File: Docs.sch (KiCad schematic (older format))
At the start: 0 parts

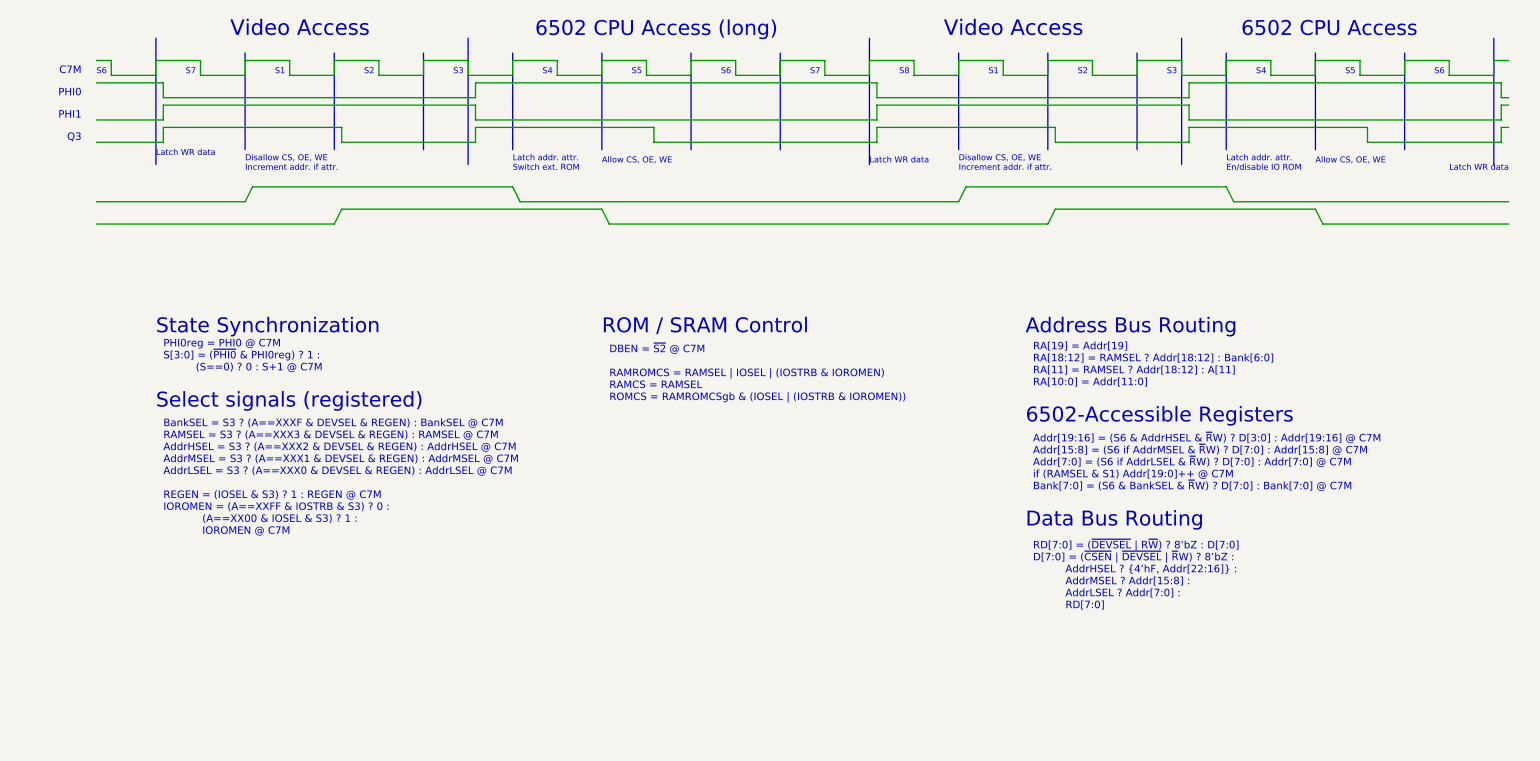
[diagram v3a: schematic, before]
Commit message: Changed libraries
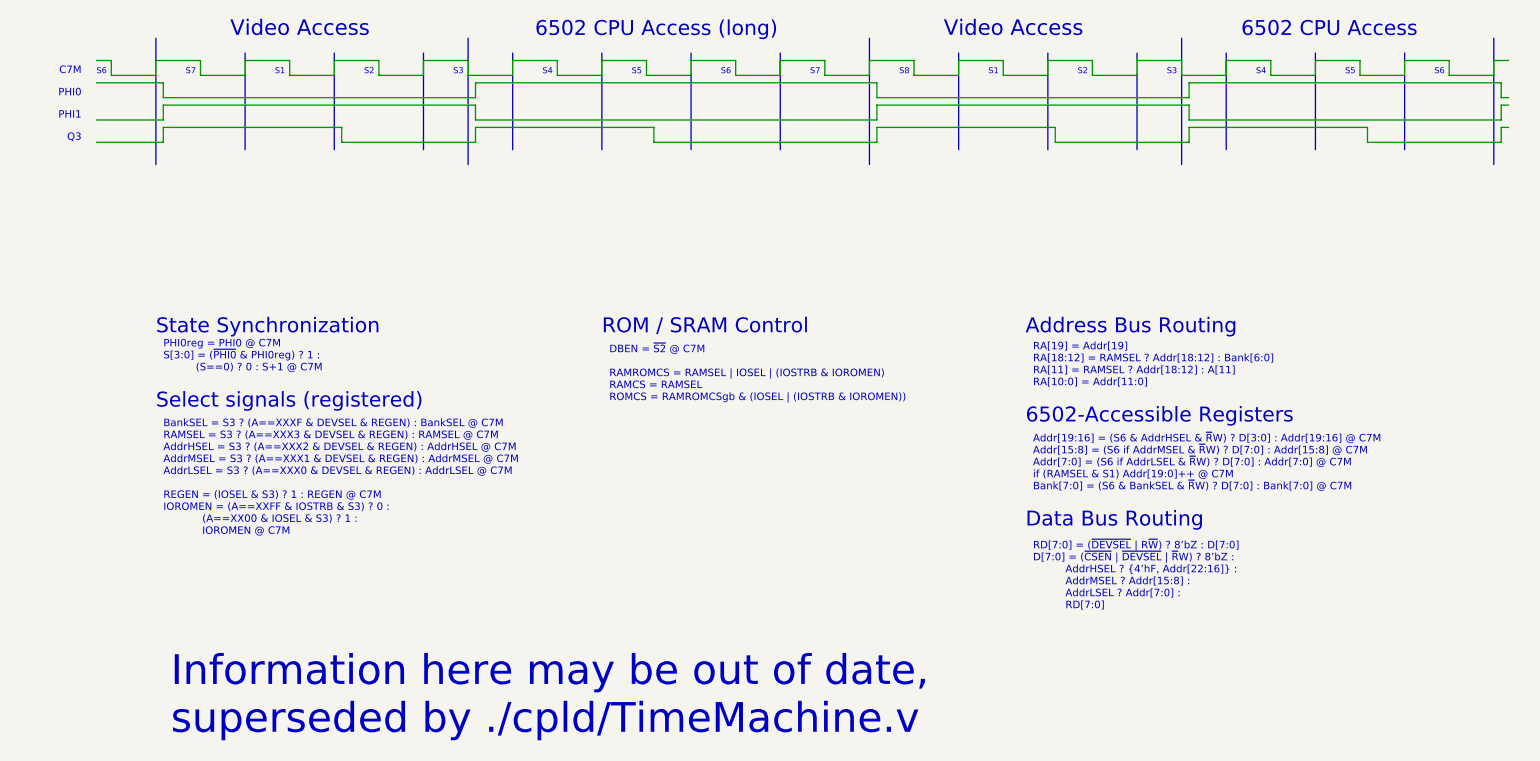
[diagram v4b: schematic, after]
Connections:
- wire segments 124 -> 106
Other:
- note added: "Information here may be out of date,\nsuperseded by ./cpld/TimeMachine.v"
- note removed: "Allow CS, OE, WE"
- note removed: "Disallow CS, OE, WE\nIncrement addr. if attr."
- note removed: "Latch WR data"
- note removed: "Latch addr. attr.\nEn/disable IO ROM"
- note removed: "Latch addr. attr.\nSwitch ext. ROM"
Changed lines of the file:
@@
 encoding utf-8
 Sheet 2 2
-Title "GR8RAM"
-Date "2019-07-23"
-Rev "0.1"
+Title "Time Machine"
+Date "2019-10-13"
+Rev "0.9"
 Comp "Garrett's Workshop"
 Comment1 ""
@@
 Wire Bus Line
 	4900 950  4900 1600
-Text Notes 4300 1700 0    40   ~ 0
-Allow CS, OE, WE
 Text Notes 1500 1100 0    40   ~ 0
 S7
@@
 Wire Bus Line
 	6100 850  6100 1700
-Text Notes 6100 1700 0    40   ~ 0
-Latch WR data
 Text Notes 6300 1100 0    40   ~ 0
 S8
@@
 Text Notes 8100 1100 0    40   ~ 0
 S3
-Text Notes 9100 1700 0    40   ~ 0
-Allow CS, OE, WE
 Text Notes 8700 1100 0    40   ~ 0
 S4
@@
 Wire Bus Line
 	1300 850  1300 1700
-Text Notes 1300 1650 0    40   ~ 0
-Latch WR data
 Text Notes 5100 1100 0    40   ~ 0
 S6
@@
 Wire Wire Line
 	5200 1000 5200 1100
+Wire Wire Line
+	10300 1000 10400 1000
+Wire Wire Line
+	10350 1250 10400 1250
+Wire Wire Line
+	10350 1300 10400 1300
+Wire Wire Line
+	10350 1450 10400 1450
+Text Notes 4350 3300 0    50   ~ 0
+DBEN = ~S2~ @ C7M\n\nRAMROMCS = RAMSEL | IOSEL | (IOSTRB & IOROMEN)\nRAMCS = RAMSEL\nROMCS = RAMROMCSgb & (IOSEL | (IOSTRB & IOROMEN))
+Text Notes 7200 3900 0    50   ~ 0
+Addr[19:16] = (S6 & AddrHSEL & ~R~W) ? D[3:0] : Addr[19:16] @ C7M\nAddr[15:8] = (S6 if AddrMSEL & ~R~W) ? D[7:0] : Addr[15:8] @ C7M\nAddr[7:0] = (S6 if AddrLSEL & ~R~W) ? D[7:0] : Addr[7:0] @ C7M\nif (RAMSEL & S1) Addr[19:0]++ @ C7M\nBank[7:0] = (S6 & BankSEL & ~R~W) ? D[7:0] : Bank[7:0] @ C7M
+Text Notes 7200 4700 0    50   ~ 0
+RD[7:0] = (~DEVSEL~ | R~W~) ? 8’bZ : D[7:0]\nD[7:0] = (~CSEN~ | ~DEVSEL~ | ~R~W) ? 8’bZ :\n          AddrHSEL ? {4’hF, Addr[22:16]} : \n          AddrMSEL ? Addr[15:8] : \n          AddrLSEL ? Addr[7:0] :\n          RD[7:0]
+Text Notes 7150 4150 0    100  ~ 0
+Data Bus Routing
+Text Notes 7150 3450 0    100  ~ 0
+6502-Accessible Registers
+Text Notes 7200 3200 0    50   ~ 0
+RA[19] = Addr[19]\nRA[18:12] = RAMSEL ? Addr[18:12] : Bank[6:0]\nRA[11] = RAMSEL ? Addr[18:12] : A[11]\nRA[10:0] = Addr[11:0]
+Text Notes 7150 2850 0    100  ~ 0
+Address Bus Routing
+Text Notes 1350 4200 0    50   ~ 0
+BankSEL = S3 ? (A==XXXF & DEVSEL & REGEN) : BankSEL @ C7M\nRAMSEL = S3 ? (A==XXX3 & DEVSEL & REGEN) : RAMSEL @ C7M\nAddrHSEL = S3 ? (A==XXX2 & DEVSEL & REGEN) : AddrHSEL @ C7M\nAddrMSEL = S3 ? (A==XXX1 & DEVSEL & REGEN) : AddrMSEL @ C7M\nAddrLSEL = S3 ? (A==XXX0 & DEVSEL & REGEN) : AddrLSEL @ C7M\n\nREGEN = (IOSEL & S3) ? 1 : REGEN @ C7M\nIOROMEN = (A==XXFF & IOSTRB & S3) ? 0 :\n            (A==XX00 & IOSEL & S3) ? 1 :\n            IOROMEN @ C7M
+Text Notes 4300 2850 0    100  ~ 0
+ROM / SRAM Control
+Text Notes 1300 2850 0    100  ~ 0
+State Synchronization
+Text Notes 1300 3350 0    100  ~ 0
+Select signals (registered)
 Text Notes 1350 3100 0    50   ~ 0
 PHI0reg = PHI0 @ C7M\nS[3:0] = (~PHI0~ & PHI0reg) ? 1 : \n          (S==0) ? 0 : S+1 @ C7M
-Text Notes 1300 3350 0    100  ~ 0
-Select signals (registered)
-Text Notes 1300 2850 0    100  ~ 0
-State Synchronization
-Text Notes 4300 2850 0    100  ~ 0
-ROM / SRAM Control
-Text Notes 1350 4200 0    50   ~ 0
-BankSEL = S3 ? (A==XXXF & DEVSEL & REGEN) : BankSEL @ C7M\nRAMSEL = S3 ? (A==XXX3 & DEVSEL & REGEN) : RAMSEL @ C7M\nAddrHSEL = S3 ? (A==XXX2 & DEVSEL & REGEN) : AddrHSEL @ C7M\nAddrMSEL = S3 ? (A==XXX1 & DEVSEL & REGEN) : AddrMSEL @ C7M\nAddrLSEL = S3 ? (A==XXX0 & DEVSEL & REGEN) : AddrLSEL @ C7M\n\nREGEN = (IOSEL & S3) ? 1 : REGEN @ C7M\nIOROMEN = (A==XXFF & IOSTRB & S3) ? 0 :\n            (A==XX00 & IOSEL & S3) ? 1 :\n            IOROMEN @ C7M
-Text Notes 7150 2850 0    100  ~ 0
-Address Bus Routing
-Wire Wire Line
-	10300 1000 10400 1000
-Wire Wire Line
-	10350 1250 10400 1250
-Wire Wire Line
-	10350 1300 10400 1300
-Wire Wire Line
-	10350 1450 10400 1450
-Text Notes 7200 3200 0    50   ~ 0
-RA[19] = Addr[19]\nRA[18:12] = RAMSEL ? Addr[18:12] : Bank[6:0]\nRA[11] = RAMSEL ? Addr[18:12] : A[11]\nRA[10:0] = Addr[11:0]
-Text Notes 10000 1750 0    40   ~ 0
-Latch WR data
-Text Notes 1900 1750 0    40   ~ 0
-Disallow CS, OE, WE\nIncrement addr. if attr.
-Text Notes 6700 1750 0    40   ~ 0
-Disallow CS, OE, WE\nIncrement addr. if attr.
-Text Notes 3700 1750 0    40   ~ 0
-Latch addr. attr.\nSwitch ext. ROM
-Text Notes 8500 1750 0    40   ~ 0
-Latch addr. attr.\nEn/disable IO ROM
-Text Notes 7150 3450 0    100  ~ 0
-6502-Accessible Registers
-Text Notes 7150 4150 0    100  ~ 0
-Data Bus Routing
-Text Notes 7200 4700 0    50   ~ 0
-RD[7:0] = (~DEVSEL~ | R~W~) ? 8’bZ : D[7:0]\nD[7:0] = (~CSEN~ | ~DEVSEL~ | ~R~W) ? 8’bZ :\n          AddrHSEL ? {4’hF, Addr[22:16]} : \n          AddrMSEL ? Addr[15:8] : \n          AddrLSEL ? Addr[7:0] :\n          RD[7:0]
-Text Notes 7200 3900 0    50   ~ 0
-Addr[19:16] = (S6 & AddrHSEL & ~R~W) ? D[3:0] : Addr[19:16] @ C7M\nAddr[15:8] = (S6 if AddrMSEL & ~R~W) ? D[7:0] : Addr[15:8] @ C7M\nAddr[7:0] = (S6 if AddrLSEL & ~R~W) ? D[7:0] : Addr[7:0] @ C7M\nif (RAMSEL & S1) Addr[19:0]++ @ C7M\nBank[7:0] = (S6 & BankSEL & ~R~W) ? D[7:0] : Bank[7:0] @ C7M
-Text Notes 4350 3300 0    50   ~ 0
-DBEN = ~S2~ @ C7M\n\nRAMROMCS = RAMSEL | IOSEL | (IOSTRB & IOROMEN)\nRAMCS = RAMSEL\nROMCS = RAMROMCSgb & (IOSEL | (IOSTRB & IOROMEN))
-Wire Wire Line
-	3700 1850 3750 1950
-Wire Wire Line
-	3750 1950 6700 1950
-Wire Wire Line
-	6700 1950 6750 1850
-Wire Wire Line
-	6750 1850 8500 1850
-Wire Wire Line
-	8500 1850 8550 1950
-Wire Wire Line
-	8550 1950 10400 1950
-Wire Wire Line
-	1950 1850 3700 1850
-Wire Wire Line
-	1950 1850 1900 1950
-Wire Wire Line
-	1900 1950 900  1950
-Wire Wire Line
-	4300 2000 4350 2100
-Wire Wire Line
-	4350 2100 7300 2100
-Wire Wire Line
-	7300 2100 7350 2000
-Wire Wire Line
-	7350 2000 9100 2000
-Wire Wire Line
-	9100 2000 9150 2100
-Wire Wire Line
-	9150 2100 10400 2100
-Wire Wire Line
-	2550 2000 4300 2000
-Wire Wire Line
-	2550 2000 2500 2100
-Wire Wire Line
-	900  2100 2500 2100
+Text Notes 1400 5550 0    200  ~ 0
+Information here may be out of date,\nsuperseded by ./cpld/TimeMachine.v
 $EndSCHEMATC

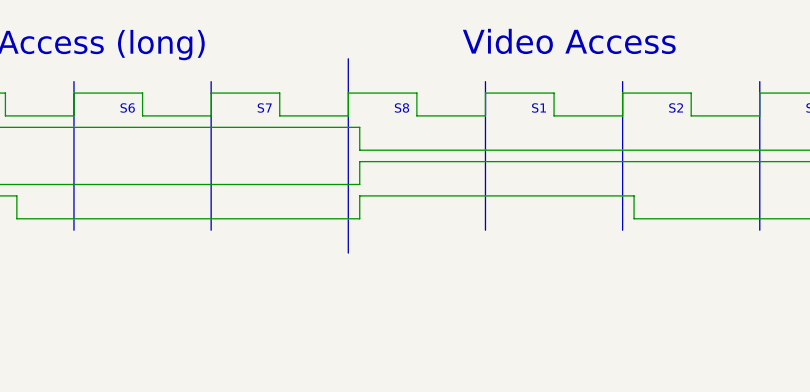
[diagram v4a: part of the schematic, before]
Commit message: New PLD revision
For write operations, register data is latched in the middle of S6, 70ns before the end of PHI0. This gives more write data setup time, which may be needed on the Apple II with the 1 MHz 6502.
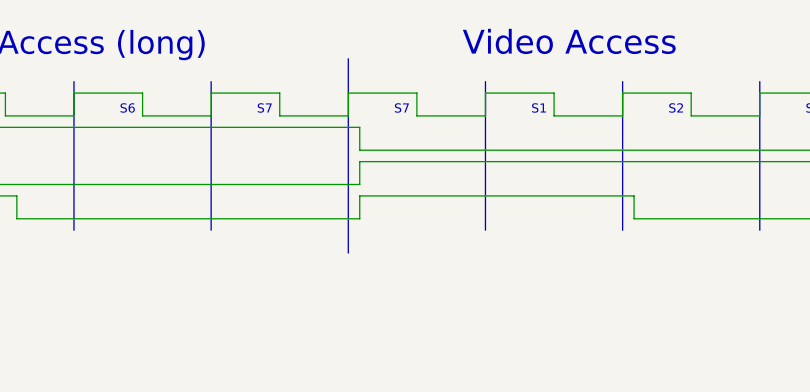
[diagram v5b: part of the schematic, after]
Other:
- note removed: "S8"
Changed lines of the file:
@@
 	6100 850  6100 1700
 Text Notes 6300 1100 0    40   ~ 0
-S8
+S7
 Wire Wire Line
 	10300 1100 10300 1000
@@
 Wire Wire Line
 	10350 1450 10400 1450
+Text Notes 1400 5550 0    200  ~ 0
+Information here may be out of date,\nsuperseded by ./cpld/TimeMachine.v
+Text Notes 1350 3100 0    50   ~ 0
+PHI0reg = PHI0 @ C7M\nS[3:0] = (~PHI0~ & PHI0reg) ? 1 : \n          (S==0) ? 0 : S+1 @ C7M
+Text Notes 1300 3350 0    100  ~ 0
+Select signals (registered)
+Text Notes 1300 2850 0    100  ~ 0
+State Synchronization
+Text Notes 4300 2850 0    100  ~ 0
+ROM / SRAM Control
+Text Notes 1350 4200 0    50   ~ 0
+BankSEL = S3 ? (A==XXXF & DEVSEL & REGEN) : BankSEL @ C7M\nRAMSEL = S3 ? (A==XXX3 & DEVSEL & REGEN) : RAMSEL @ C7M\nAddrHSEL = S3 ? (A==XXX2 & DEVSEL & REGEN) : AddrHSEL @ C7M\nAddrMSEL = S3 ? (A==XXX1 & DEVSEL & REGEN) : AddrMSEL @ C7M\nAddrLSEL = S3 ? (A==XXX0 & DEVSEL & REGEN) : AddrLSEL @ C7M\n\nREGEN = (IOSEL & S3) ? 1 : REGEN @ C7M\nIOROMEN = (A==XXFF & IOSTRB & S3) ? 0 :\n            (A==XX00 & IOSEL & S3) ? 1 :\n            IOROMEN @ C7M
+Text Notes 7150 2850 0    100  ~ 0
+Address Bus Routing
+Text Notes 7200 3200 0    50   ~ 0
+RA[19] = Addr[19]\nRA[18:12] = RAMSEL ? Addr[18:12] : Bank[6:0]\nRA[11] = RAMSEL ? Addr[18:12] : A[11]\nRA[10:0] = Addr[11:0]
+Text Notes 7150 3450 0    100  ~ 0
+6502-Accessible Registers
+Text Notes 7150 4150 0    100  ~ 0
+Data Bus Routing
+Text Notes 7200 4700 0    50   ~ 0
+RD[7:0] = (~DEVSEL~ | R~W~) ? 8’bZ : D[7:0]\nD[7:0] = (~CSEN~ | ~DEVSEL~ | ~R~W) ? 8’bZ :\n          AddrHSEL ? {4’hF, Addr[22:16]} : \n          AddrMSEL ? Addr[15:8] : \n          AddrLSEL ? Addr[7:0] :\n          RD[7:0]
+Text Notes 7200 3900 0    50   ~ 0
+Addr[19:16] = (S6 & AddrHSEL & ~R~W) ? D[3:0] : Addr[19:16] @ C7M\nAddr[15:8] = (S6 if AddrMSEL & ~R~W) ? D[7:0] : Addr[15:8] @ C7M\nAddr[7:0] = (S6 if AddrLSEL & ~R~W) ? D[7:0] : Addr[7:0] @ C7M\nif (RAMSEL & S1) Addr[19:0]++ @ C7M\nBank[7:0] = (S6 & BankSEL & ~R~W) ? D[7:0] : Bank[7:0] @ C7M
 Text Notes 4350 3300 0    50   ~ 0
 DBEN = ~S2~ @ C7M\n\nRAMROMCS = RAMSEL | IOSEL | (IOSTRB & IOROMEN)\nRAMCS = RAMSEL\nROMCS = RAMROMCSgb & (IOSEL | (IOSTRB & IOROMEN))
-Text Notes 7200 3900 0    50   ~ 0
-Addr[19:16] = (S6 & AddrHSEL & ~R~W) ? D[3:0] : Addr[19:16] @ C7M\nAddr[15:8] = (S6 if AddrMSEL & ~R~W) ? D[7:0] : Addr[15:8] @ C7M\nAddr[7:0] = (S6 if AddrLSEL & ~R~W) ? D[7:0] : Addr[7:0] @ C7M\nif (RAMSEL & S1) Addr[19:0]++ @ C7M\nBank[7:0] = (S6 & BankSEL & ~R~W) ? D[7:0] : Bank[7:0] @ C7M
-Text Notes 7200 4700 0    50   ~ 0
-RD[7:0] = (~DEVSEL~ | R~W~) ? 8’bZ : D[7:0]\nD[7:0] = (~CSEN~ | ~DEVSEL~ | ~R~W) ? 8’bZ :\n          AddrHSEL ? {4’hF, Addr[22:16]} : \n          AddrMSEL ? Addr[15:8] : \n          AddrLSEL ? Addr[7:0] :\n          RD[7:0]
-Text Notes 7150 4150 0    100  ~ 0
-Data Bus Routing
-Text Notes 7150 3450 0    100  ~ 0
-6502-Accessible Registers
-Text Notes 7200 3200 0    50   ~ 0
-RA[19] = Addr[19]\nRA[18:12] = RAMSEL ? Addr[18:12] : Bank[6:0]\nRA[11] = RAMSEL ? Addr[18:12] : A[11]\nRA[10:0] = Addr[11:0]
-Text Notes 7150 2850 0    100  ~ 0
-Address Bus Routing
-Text Notes 1350 4200 0    50   ~ 0
-BankSEL = S3 ? (A==XXXF & DEVSEL & REGEN) : BankSEL @ C7M\nRAMSEL = S3 ? (A==XXX3 & DEVSEL & REGEN) : RAMSEL @ C7M\nAddrHSEL = S3 ? (A==XXX2 & DEVSEL & REGEN) : AddrHSEL @ C7M\nAddrMSEL = S3 ? (A==XXX1 & DEVSEL & REGEN) : AddrMSEL @ C7M\nAddrLSEL = S3 ? (A==XXX0 & DEVSEL & REGEN) : AddrLSEL @ C7M\n\nREGEN = (IOSEL & S3) ? 1 : REGEN @ C7M\nIOROMEN = (A==XXFF & IOSTRB & S3) ? 0 :\n            (A==XX00 & IOSEL & S3) ? 1 :\n            IOROMEN @ C7M
-Text Notes 4300 2850 0    100  ~ 0
-ROM / SRAM Control
-Text Notes 1300 2850 0    100  ~ 0
-State Synchronization
-Text Notes 1300 3350 0    100  ~ 0
-Select signals (registered)
-Text Notes 1350 3100 0    50   ~ 0
-PHI0reg = PHI0 @ C7M\nS[3:0] = (~PHI0~ & PHI0reg) ? 1 : \n          (S==0) ? 0 : S+1 @ C7M
-Text Notes 1400 5550 0    200  ~ 0
-Information here may be out of date,\nsuperseded by ./cpld/TimeMachine.v
 $EndSCHEMATC
